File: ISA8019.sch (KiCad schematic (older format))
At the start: 55 parts, among them J1 Bus_ISA_16bit, J2 8P8C_Shielded, J4 Jumper mode, J5 PNP force, J6 BROM size and base address, J7 I/O base address, J8 Medium type, J9 IRQ select, T1 13F-39MNL, U1 RTL8019AS, U2 AT93C46DN, U3 SST39SF010 / MX29F001T, Y1 20MHz

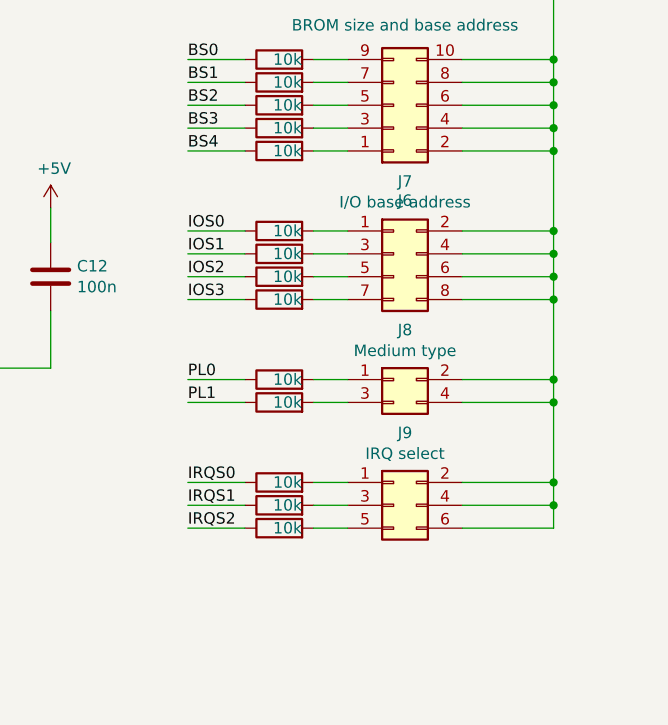
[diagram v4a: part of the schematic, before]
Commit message: Add silkscreen and jumper settings
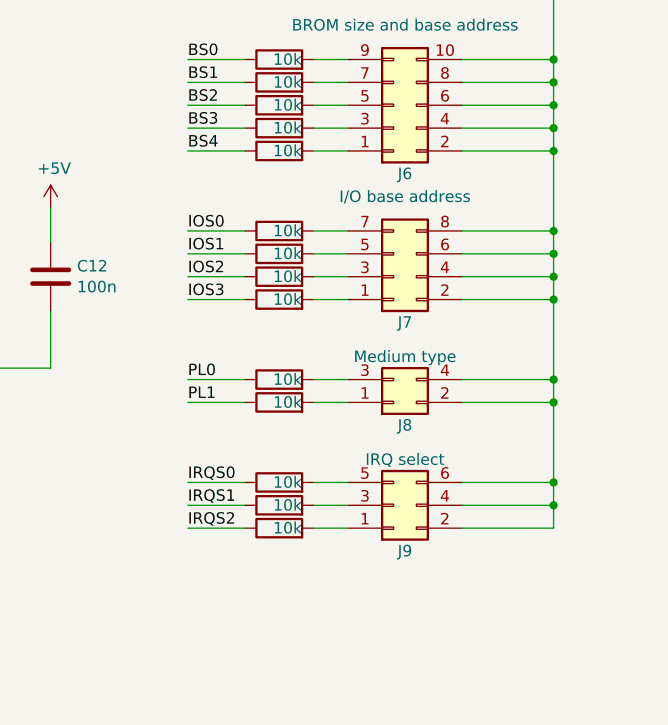
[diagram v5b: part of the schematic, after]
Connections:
- net at J7.1 (Pin_1): now also R17.2; no longer R14.2
- net at J7.3 (Pin_3): now also R16.2; no longer R15.2
- net at J7.5 (Pin_5): now also R15.2; no longer R16.2
- net at J7.7 (Pin_7): now also R14.2; no longer R17.2
- net at J8.1 (Pin_1): now also R19.2; no longer R18.2
- net at J8.3 (Pin_3): now also R18.2; no longer R19.2
- net at J9.1 (Pin_1): now also R22.2; no longer R20.2
- net at J9.5 (Pin_5): now also R20.2; no longer R22.2
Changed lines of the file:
@@
 U 1 1 605952D4
 P 14850 2650
-F 0 "J6" H 14900 3067 50  0000 C CNN
+F 0 "J6" H 14900 2950 50  0000 C CNN
 F 1 "BROM size and base address" H 14900 2300 50  0000 C CNN
 F 2 "Connector_PinHeader_2.54mm:PinHeader_2x05_P2.54mm_Vertical" H 14850 2650 50  0001 C CNN
@@
 L Connector_Generic:Conn_02x04_Odd_Even J7
 U 1 1 605EB97F
-P 14850 3300
-F 0 "J7" H 14900 3617 50  0000 C CNN
-F 1 "I/O base address" H 14900 3526 50  0000 C CNN
-F 2 "Connector_PinHeader_2.54mm:PinHeader_2x04_P2.54mm_Vertical" H 14850 3300 50  0001 C CNN
-F 3 "~" H 14850 3300 50  0001 C CNN
-	1    14850 3300
-	1    0    0    -1
+P 14850 3400
+F 0 "J7" H 14900 3600 50  0000 C CNN
+F 1 "I/O base address" H 14900 3050 50  0000 C CNN
+F 2 "Connector_PinHeader_2.54mm:PinHeader_2x04_P2.54mm_Vertical" H 14850 3400 50  0001 C CNN
+F 3 "~" H 14850 3400 50  0001 C CNN
+	1    14850 3400
+	1    0    0    1
 $EndComp
 $Comp
 L Connector_Generic:Conn_02x02_Odd_Even J8
 U 1 1 605ED14C
-P 14850 3850
-F 0 "J8" H 14900 4067 50  0000 C CNN
-F 1 "Medium type" H 14900 3976 50  0000 C CNN
-F 2 "Connector_PinHeader_2.54mm:PinHeader_2x02_P2.54mm_Vertical" H 14850 3850 50  0001 C CNN
-F 3 "~" H 14850 3850 50  0001 C CNN
-	1    14850 3850
-	1    0    0    -1
+P 14850 3950
+F 0 "J8" H 14900 4050 50  0000 C CNN
+F 1 "Medium type" H 14900 3750 50  0000 C CNN
+F 2 "Connector_PinHeader_2.54mm:PinHeader_2x02_P2.54mm_Vertical" H 14850 3950 50  0001 C CNN
+F 3 "~" H 14850 3950 50  0001 C CNN
+	1    14850 3950
+	1    0    0    1
 $EndComp
 $Comp
@@
 U 1 1 605EED03
 P 14850 4400
-F 0 "J9" H 14900 4717 50  0000 C CNN
-F 1 "IRQ select" H 14900 4626 50  0000 C CNN
+F 0 "J9" H 14900 4600 50  0000 C CNN
+F 1 "IRQ select" H 14900 4200 50  0000 C CNN
 F 2 "Connector_PinHeader_2.54mm:PinHeader_2x03_P2.54mm_Vertical" H 14850 4400 50  0001 C CNN
 F 3 "~" H 14850 4400 50  0001 C CNN
 	1    14850 4400
-	1    0    0    -1
+	1    0    0    1
 $EndComp
 $Comp

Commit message: Add JLC markings, manufacturing details and new gerbers
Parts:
- added H5: OSHW Logo, Symbol:OSHW-Logo_11.4x12mm_Copper, symbol Mechanical:MountingHole
- J1: footprint Connector_PCBEdge:BUS_AT -> Bus_AT_without_Silkscreen:BUS_AT_WO_SILKSCREEN
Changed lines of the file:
@@
 F 0 "J1" H 3000 6767 50  0000 C CNN
 F 1 "Bus_ISA_16bit" H 3000 6676 50  0000 C CNN
-F 2 "Connector_PCBEdge:BUS_AT" H 3000 4050 50  0001 C CNN
+F 2 "Bus_AT_without_Silkscreen:BUS_AT_WO_SILKSCREEN" H 3000 4050 50  0001 C CNN
 F 3 "https://en.wikipedia.org/wiki/Industry_Standard_Architecture" H 3000 4050 50  0001 C CNN
 	1    3000 4000
@@
 Wire Wire Line
 	12700 9450 12700 9500
+$Comp
+L Mechanical:MountingHole H5
+U 1 1 5FCDE6CF
+P 15250 9150
+F 0 "H5" H 15350 9196 50  0000 L CNN
+F 1 "OSHW Logo" H 15350 9105 50  0000 L CNN
+F 2 "Symbol:OSHW-Logo_11.4x12mm_Copper" H 15250 9150 50  0001 C CNN
+F 3 "~" H 15250 9150 50  0001 C CNN
+	1    15250 9150
+	1    0    0    -1
+$EndComp
 $EndSCHEMATC
